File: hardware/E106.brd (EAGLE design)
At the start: 38.1 x 31.9 mm, 33 parts, among them Q2 NPN, SW1 SPST_TACT-KMR2, U10 TSL2591, U11 915MHz, U5 ATMEGA328P-MU, U6 SHT35, U8 MCP1703CB, X1 16 MHz

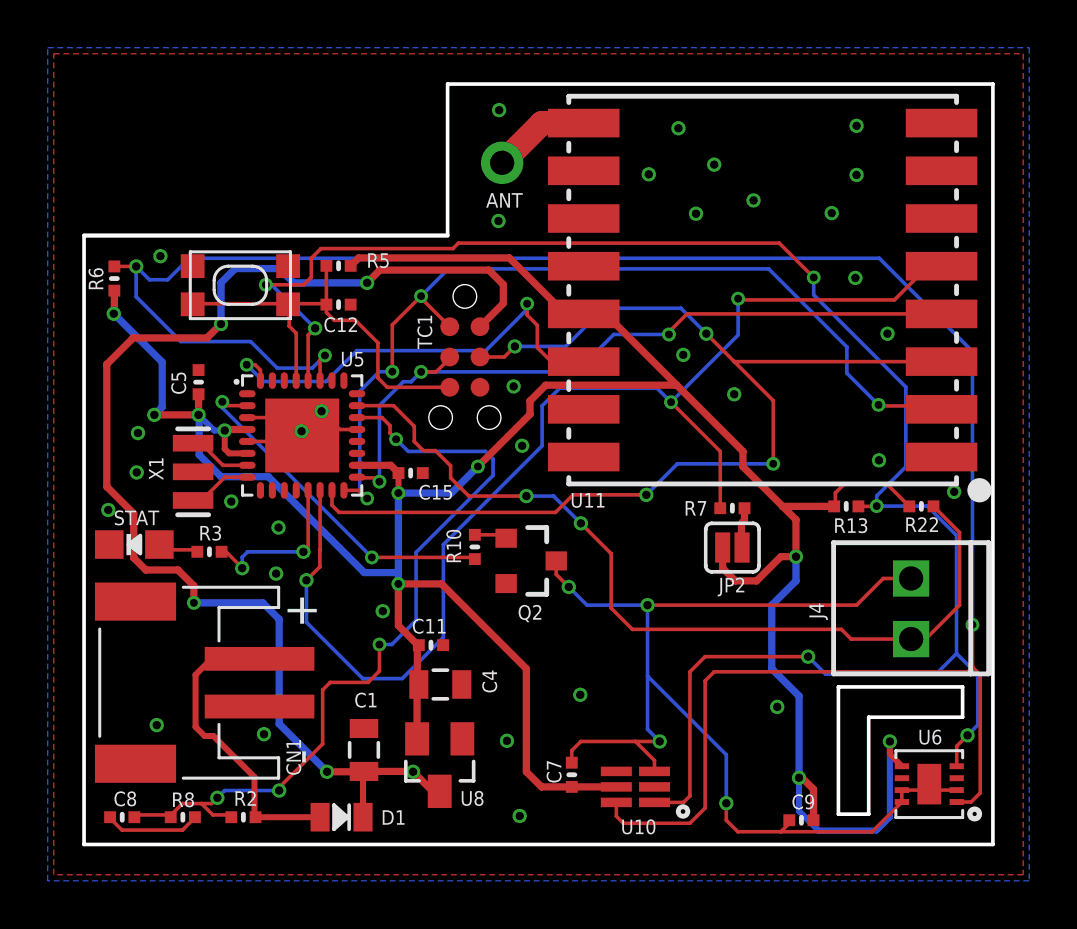
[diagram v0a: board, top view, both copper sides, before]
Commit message: v1.1.0 - hardware update
- added SPI flash
- removed jumper from radio SS
- added RGB LED instead of single LED
- trace fixes
- ERC/DRC
- Silkscreen update
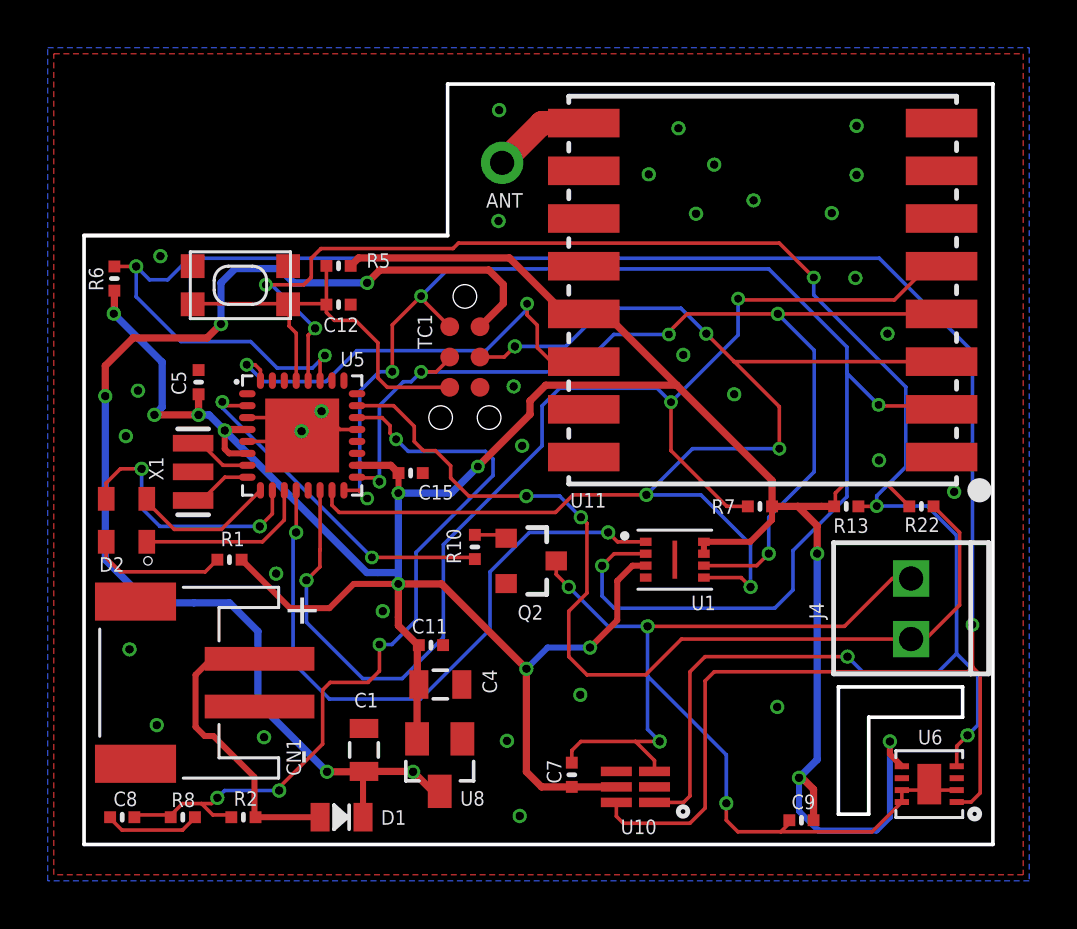
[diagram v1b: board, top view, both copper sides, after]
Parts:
- removed JP2: JUMPER-SMT_2_NC_PASTE_SILK, SparkFun-Jumpers:SMT-JUMPER_2_NC_PASTE_SILK
- removed R3: 1K, Adafruit Feather 32u4 Bluefruit LE:MICROBUILDER__0402MP
- removed STAT: BLUE, microbuilder:CHIPLED_0805_NOOUTLINE
- added D2: LTST-C19FD1WT, LTST-C19FD1WT:4-SMD
- added R1: 1K, Adafruit Feather 32u4 Bluefruit LE:MICROBUILDER__0402MP
- added U1: W25X40CLUXIG_TR, W25X40CLUXIG_TR:PSON50P300X200X60-9N
- moved R7 1.16 mm to (28.3, 58.5)
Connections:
- removed net N$11: JP2.1, R7.2
- removed net N$8: R3.1, STAT.A
- new net N$6: D2.4, R1.2
- net D5: now also D2.2
- net D6: now also D2.3
- net D7: now also D2.1
- net D8: now also U1.1
- net D9: no longer R3.2
- net GND: now also U1.4, U1.9; no longer STAT.C
- net MISO: now also U1.2
- net MOSI: now also U1.5
- net SCK: now also U1.6
- net VCC: now also R1.1, R7.2, U1.3, U1.7, U1.8; no longer JP2.2
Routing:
- net D8: track 0.00 -> 27.2 mm, vias 0 -> 2
- net MISO: track 38.3 -> 60.2 mm, vias 4 -> 5
- net SCK: track 30.9 -> 45.3 mm, vias 3 -> 5
- net VCC: track 126.4 -> 139.1 mm, vias 10 -> 12
- net D6: track 0.00 -> 11.0 mm, vias 0 -> 2
- net MOSI: track 46.2 -> 55.3 mm, vias 4 -> 5
- net D7: track 0.00 -> 7.39 mm
- net D9: track 6.99 -> 0.00 mm, vias 2 -> 0
- net D5: track 0.00 -> 6.05 mm
- net N$6: track 0.00 -> 5.78 mm
- net A0: track 36.5 -> 40.8 mm
- net N$8: track 1.73 -> 0.00 mm
- net N$11: track 1.71 -> 0.00 mm
- net SS: track 50.5 -> 51.5 mm
- net GND: vias 34 -> 32
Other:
- board text added: "v1.1.0 | October 2019"
- board text removed: "v1.0.0 | September 2018"

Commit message: minor adjustments
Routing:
- net A7: track 33.6 -> 32.5 mm
- net VBAT: track 12.9 -> 13.6 mm
